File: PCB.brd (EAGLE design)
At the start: 231 x 168.9 mm, 61 parts, among them IC1 TL082, IC2 PIC18F2550_28DIP, IC3 7812, IC4 7805, IC5 7912, IC6 TL082, K1 G5L, Q1 20 mhz, T1 BC548, X2 FUENTE

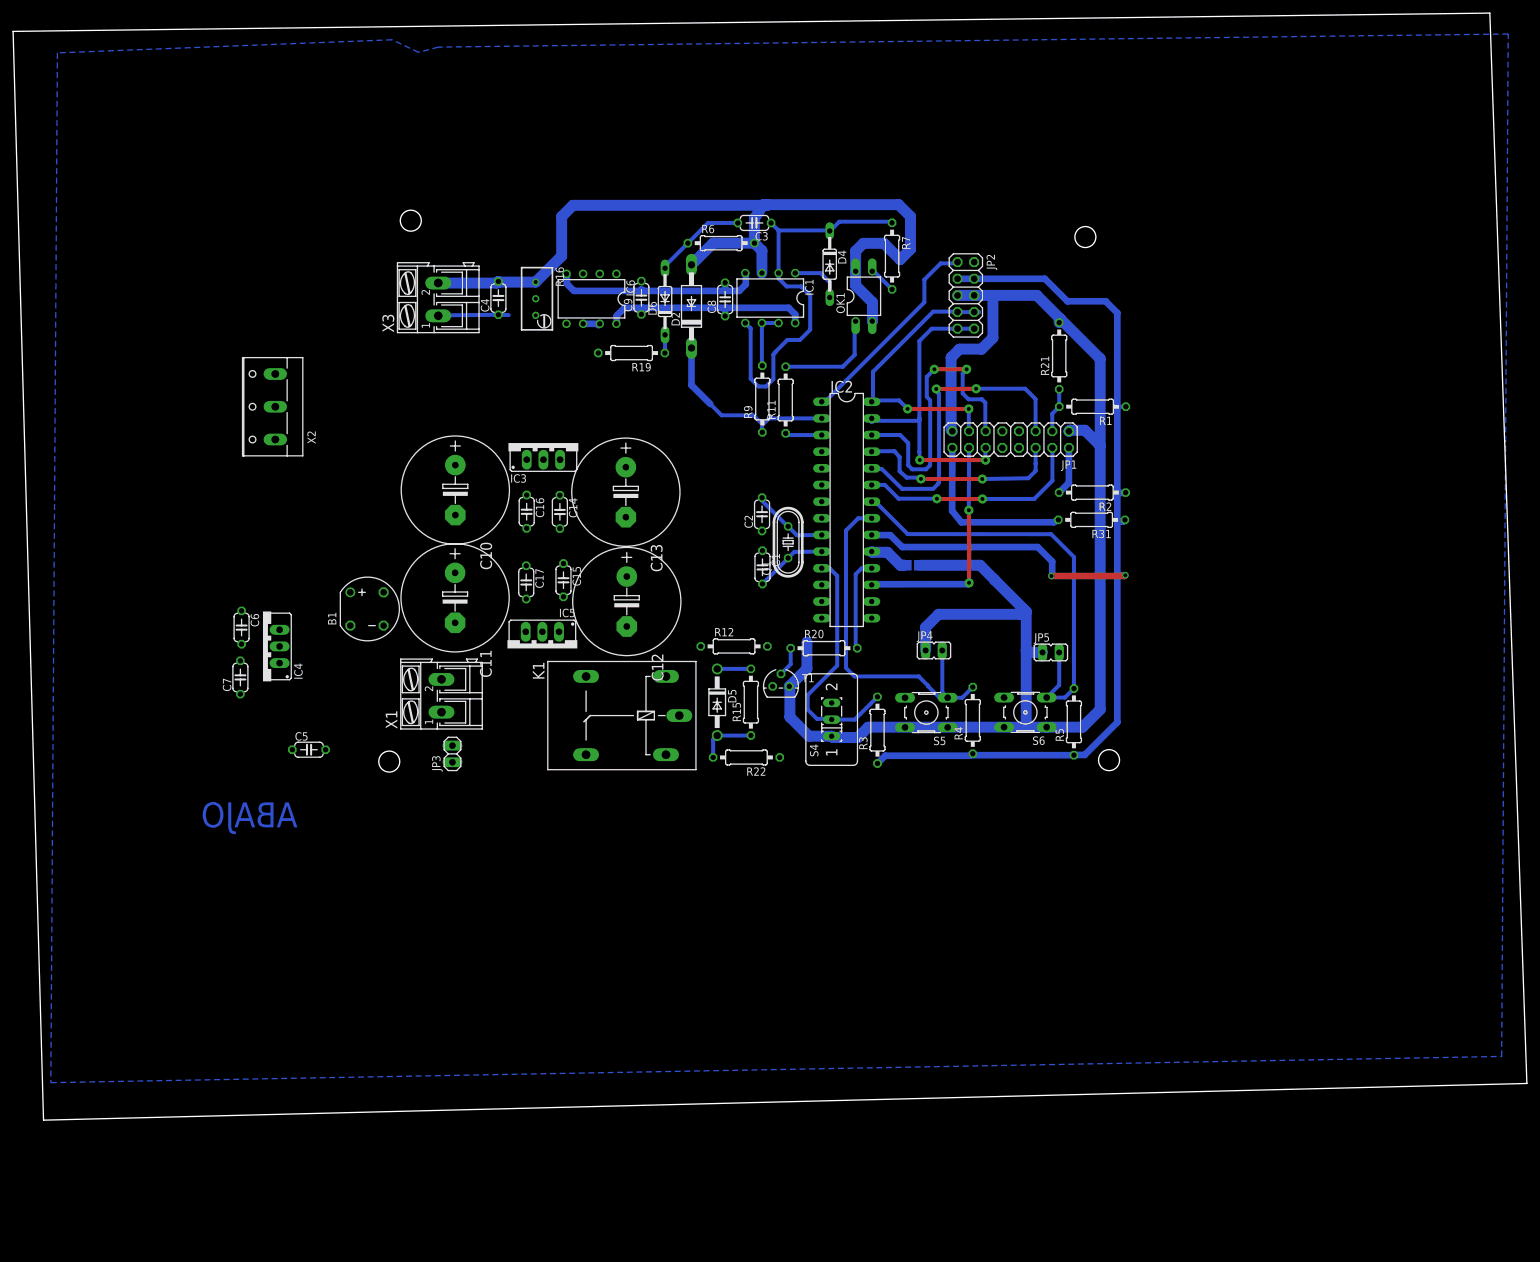
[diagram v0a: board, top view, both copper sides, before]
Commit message: Ver 2
Algorithm: I applied some filters.
Board and scheme: I implemented a balanced opamp circuit that proof to by less noisy.
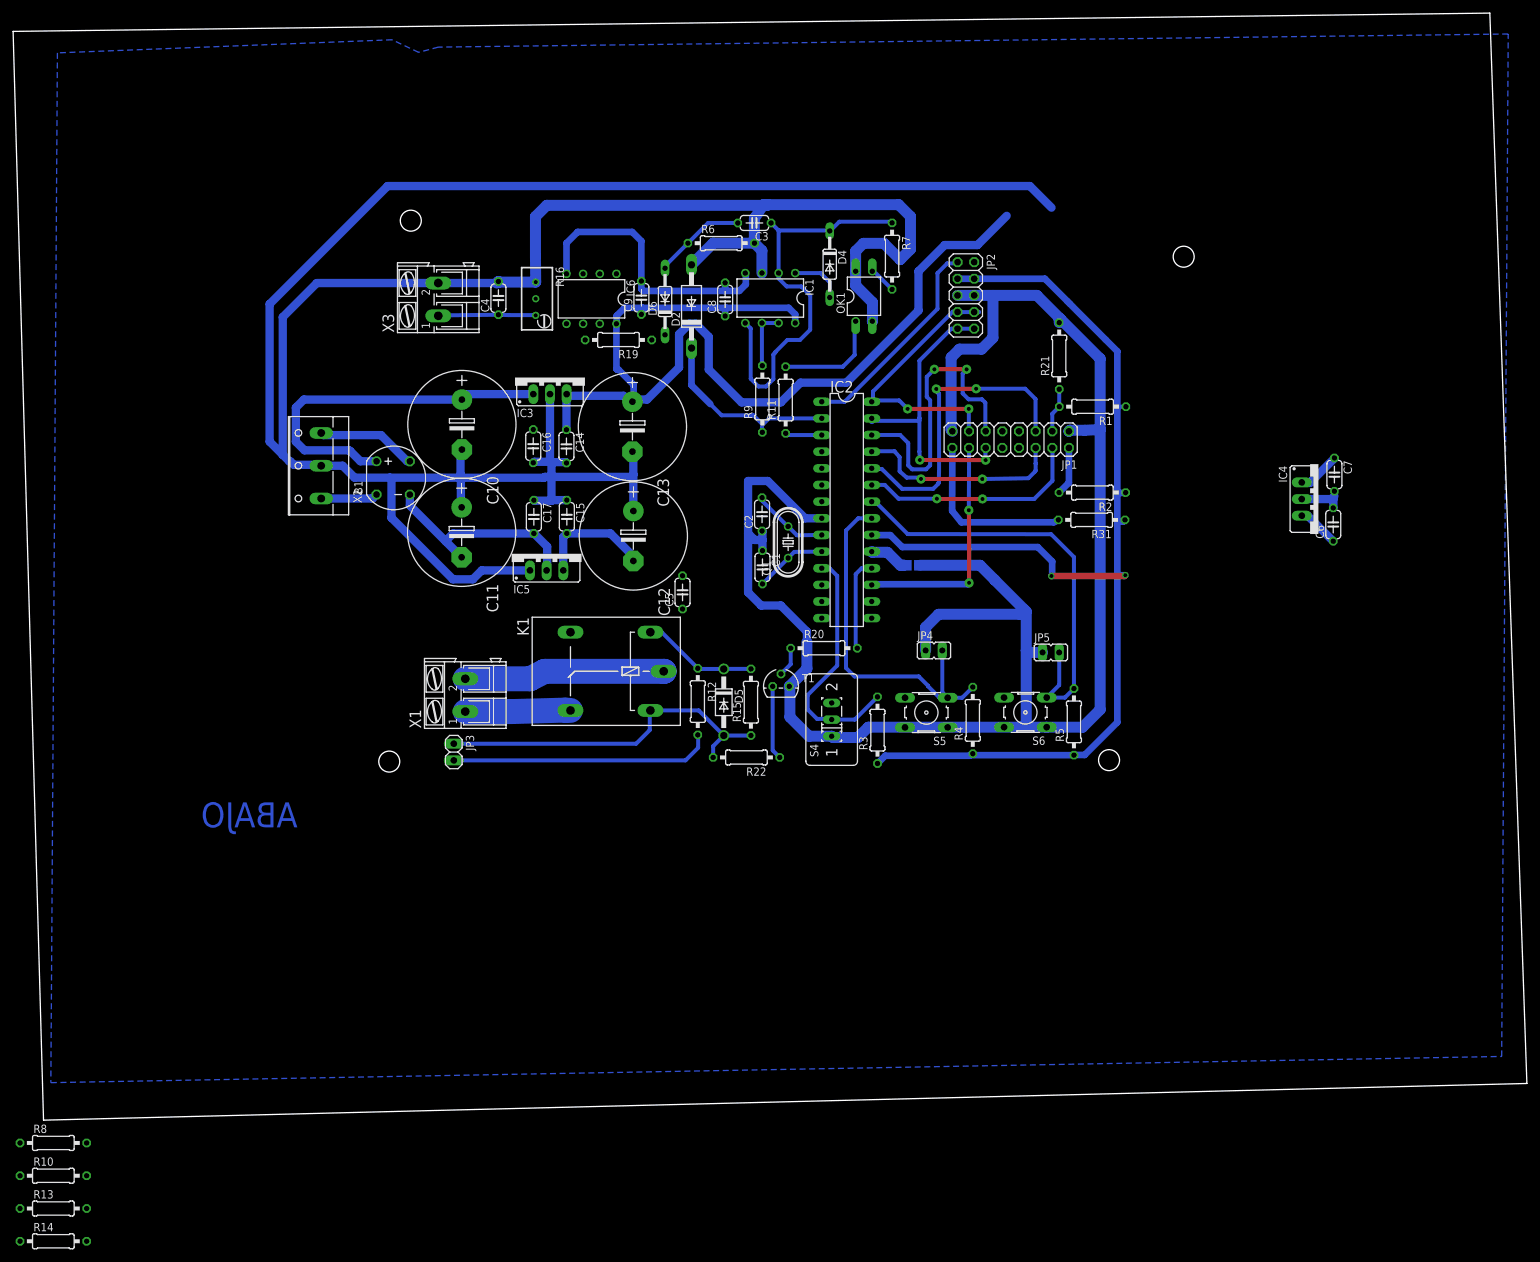
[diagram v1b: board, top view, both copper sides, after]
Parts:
- added R10, R13, R14, R8: 10k, resistor:0207/10
- moved C7 169.8 mm to (51.5, 3.98), turned to 270 degrees
- moved C6 167.3 mm to (51.3, -3.65), turned to 90 degrees
- moved IC4 162.6 mm to (49.0, 0.24), turned to 270 degrees
- moved C5 61.8 mm to (-48.0, -14.0), turned to 90 degrees
- moved B1 20.4 mm to (-92.1, 3.47)
- moved IC5 14.5 mm to (-68.7, -8.10), turned to 0 degrees
- moved X2 11.4 mm to (-104.4, 5.33)
- moved R12 10.1 mm to (-45.7, -30.7), turned to 270 degrees
- moved C17 10.1 mm to (-70.7, -2.47)
- moved IC3 10.0 mm to (-68.2, 18.8)
- moved C10 10.0 mm to (-81.7, 11.6)
- moved C11 10.0 mm to (-81.7, -4.83)
- moved C12 10.0 mm to (-55.5, -5.39)
- moved C13 10.0 mm to (-55.6, 11.3)
- moved C14 10.0 mm to (-65.7, 8.28)
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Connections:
- net GND: now also R13.2, R14.1, R16.2
- net N$1: now also IC6.3, R13.1, R14.2; no longer IC6.1, IC6.2, IC6.5
- net N$21: now also IC6.1, R8.1; no longer IC6.6, IC6.7
- net N$51: now also R10.2
- net N$7: now also IC6.2, R10.1, R8.2; no longer IC6.3, R16.2
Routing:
- net GND: track 368.8 -> 757.5 mm
- net +12V: track 37.4 -> 174.8 mm
- net N$26: track 0.00 -> 55.8 mm
- net N$36: track 8.75 -> 54.7 mm
- net N$16: track 0.00 -> 40.1 mm
- net N$31: track 0.00 -> 33.3 mm
- net N$30: track 0.00 -> 30.7 mm
- net -12V: track 33.2 -> 62.4 mm
- net N$34: track 0.00 -> 16.1 mm
- net N$33: track 0.00 -> 15.3 mm
- net N$45: track 0.00 -> 11.3 mm
- net N$32: track 0.00 -> 8.70 mm
- net N$51: track 10.8 -> 14.9 mm
- net +5V: track 176.3 -> 179.2 mm
- net N$21: track 2.86 -> 0.00 mm
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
